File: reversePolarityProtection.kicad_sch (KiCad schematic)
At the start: 4 parts, among them Q7 XPH3R114MC

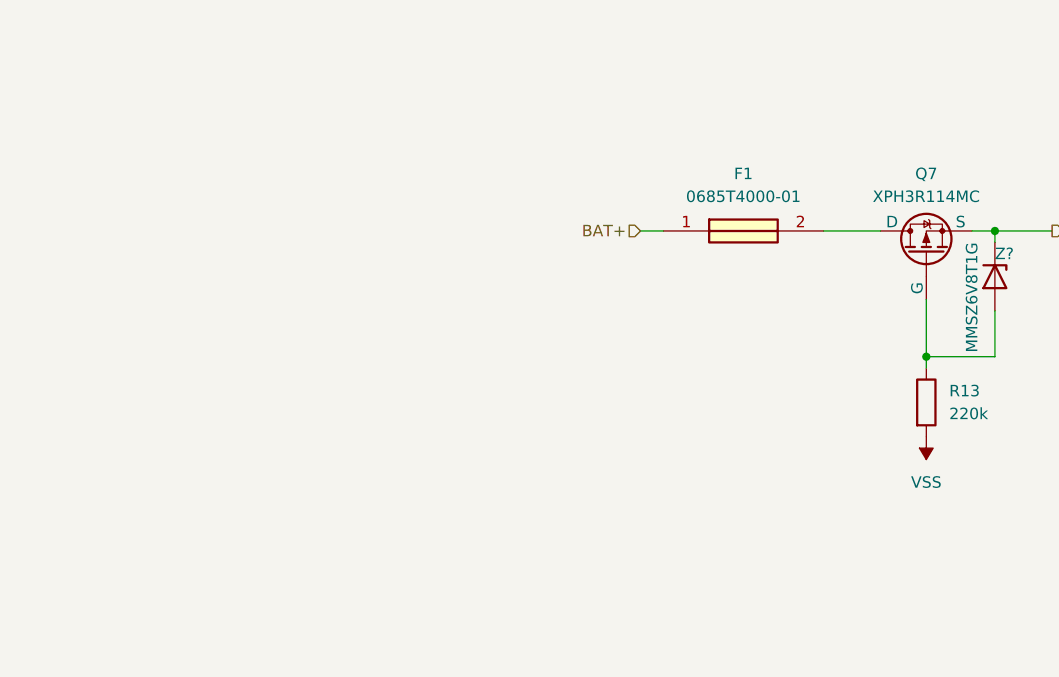
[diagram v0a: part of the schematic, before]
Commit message: Updated reverse polarity protection
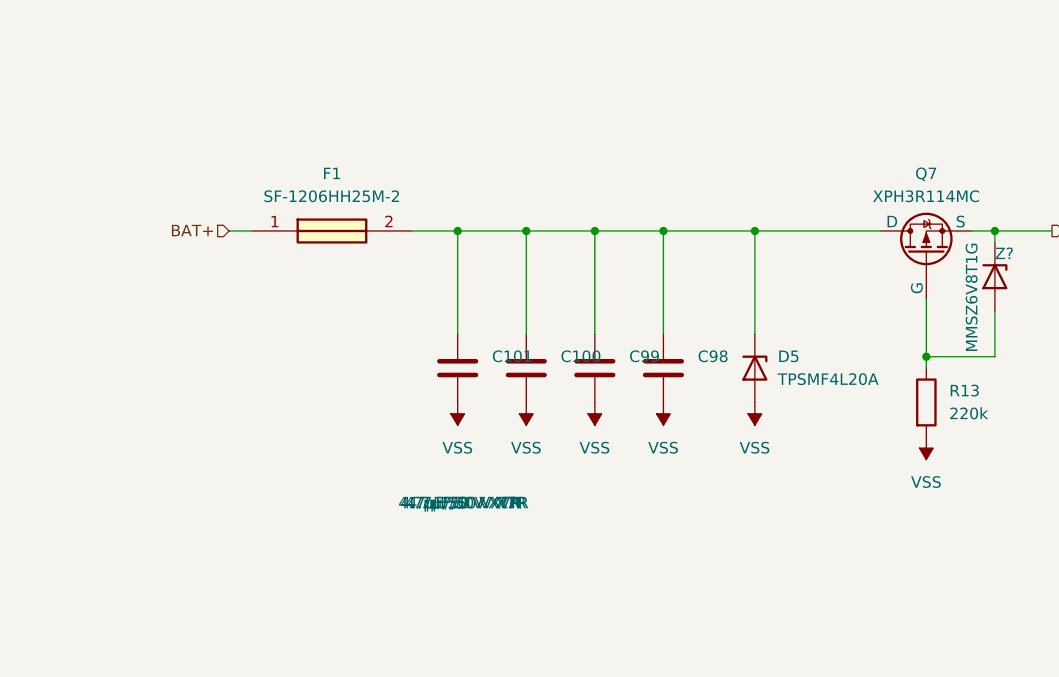
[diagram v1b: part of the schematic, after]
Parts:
- added C100, C101, C98, C99: 4.7µF/50 V X7R, Capacitor_SMD:C_1210_3225Metric, symbol Device:C
- added D5: TPSMF4L20A, symbol Device:D_Zener
- F1: value 0685T4000-01 -> SF-1206HH25M-2
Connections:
- net VSS: now also C100.2, C101.2, C98.2, C99.2, D5.2 (A)
- net at F1.2, Q7.1 (D): now also C100.1, C101.1, C98.1, C99.1, D5.1 (K)
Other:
- moved on the sheet: F1
